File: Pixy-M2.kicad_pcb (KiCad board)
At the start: 4 copper layers, 66 x 100 mm, 57 parts, among them J10 SM09B-SRSS-TB, J4 SM06B-SRSS-TB, J5 SM06B-SRSS-TB, J6 SM06B-SRSS-TB, J7 SM06B-SRSS-TB, J8 SM06B-SRSS-TB, J9 SM06B-SRSS-TB, Q1 AO4407A, SW3 JS102011SAQN, U1 ESP32-S3-DevKitC-1-N8R8, U3 AP63203WU, U4 DRV8231ADSG, U5 DRV8231ADSG

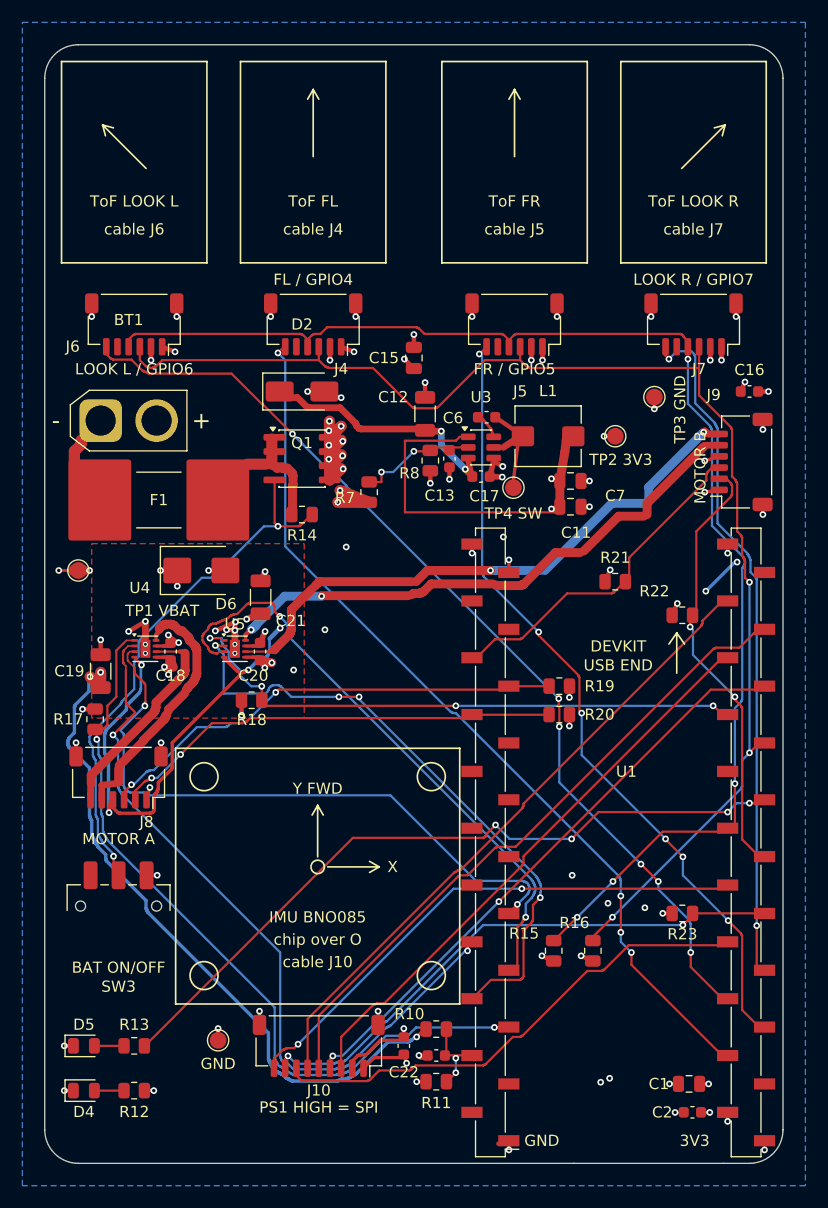
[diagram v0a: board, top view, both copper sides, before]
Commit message: layout: straighten routed copper into 0/45/90 degree runs
The A* router turns for free on its 0.05 mm grid, so any other angle came
out as a staircase of 0.05-0.3 mm steps that renders as a curve: 1060 of
the board's 1678 segments, most visibly the motor trunks round U4/U5.

New rework stage 21, tools/autoroute/octilinear.py, runs after devkit.py:
- joins pieces that meet only by overlapping, splitting the host so no
  copper moves (_heal);
- cuts each net and layer into chains between pads, vias, junctions and
  width changes, and rebuilds each as the fewest clear legs, preferring
  45 degree turns and chamfering 90 degree corners;
- tests clearance with the router's raster and the custom floors, plus
  0.02 mm, and holds 0.85 mm between IPROPI and motor copper;
- keeps each motor output within 1.5 mm of its partner, so a pair
  straightens together;
- leaves the hand-placed buck block and the piece on each U4/U5 pin, and
  keeps narrow necks inside their Motor pin escape area;
- repeats until a round changes nothing.

Result: 1678 -> 699 segments, 76 -> 15 off-angle (all hand-placed stubs).
Motor loops A 26.4 -> 25.9 mm2, B 27.8 -> 24.3 mm2. IPROPI 0.80 mm and
REG_EN 8.0 mm from motor copper, unchanged. 192 vias. DRC 0 violations /
0 unconnected / 0 parity, aperture audit passes, and a full replay
reproduces the board. Evidence in layout/octilinear/.

Docs: renders refreshed, devkit measurements updated, and CLAUDE.md's
GPIO2 floor corrected to 1.20 mm (J8's move in stage 20 set it).

Co-Authored-By: Claude Opus 5.5 <noreply@anthropic.com>
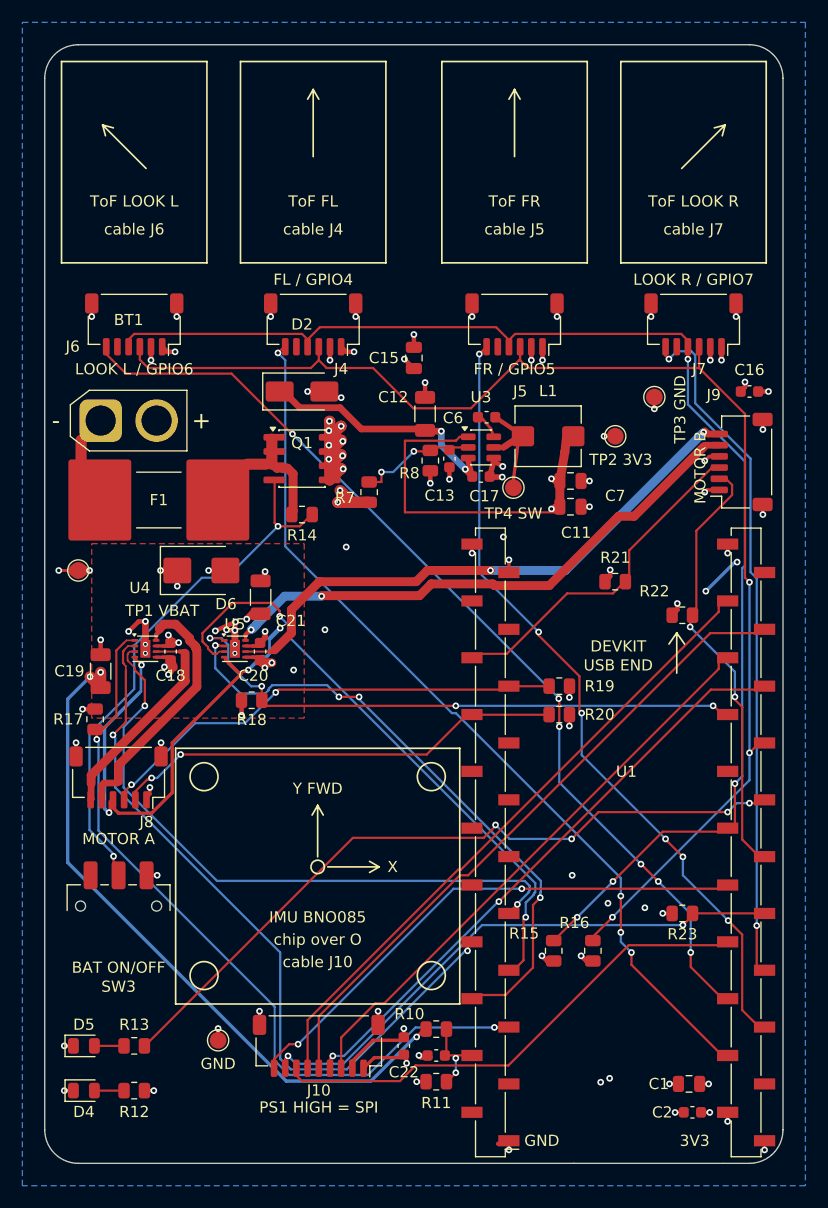
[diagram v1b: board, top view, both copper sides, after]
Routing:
- net /MOT_A_2: track 21.8 -> 23.5 mm
- net /ESP_3V3: track 102.8 -> 104.0 mm
- net /MOT_B_2: track 48.7 -> 49.8 mm
- net /GPIO42: track 55.6 -> 54.6 mm
- net /MOT_B_1: track 50.9 -> 51.7 mm
- net /VBAT: track 97.9 -> 98.7 mm
- net /GPIO40: track 66.9 -> 66.3 mm
- net GND: track 75.9 -> 76.5 mm

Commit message: power: independent motor cutoff, 1.242 V current reference, USB-priority isolation
Three supply problems on the devkit board:
- R7/R8 disable only the buck, so USB could keep the ESP32 alive and driving
  the motors from a flat pack.
- U4/U5 VREF came from the 3V3 rail, so the current limit followed the rail.
- The buck output was tied straight to the devkit's 3V3 pins, so USB and the
  buck fed one rail.

Schematic (tools/schematic/power_integrity.py; part data in
tools/power_integrity_data.py):
- U6 TLV3012B watches VBAT through R24/R25/R26 (100 k / 23.2 k / 825 k,
  0.1 %, 25 ppm/C) against its 1.242 V reference. U7 SN74LV4066A disconnects
  GPIO39-42 from the drivers below 6.35 V and reconnects them above 6.75 V,
  so the drivers' pulldowns coast both motors whatever USB or firmware do.
  The DC envelopes are 6.01-6.74 V (coast) and 6.39-7.08 V (enable).
- MOTOR_VREF from U6's REF feeds U4/U5 VREF. R17/R18 are now 1 k 1 %:
  ITRIP 0.828 A nominal, IPROPI 1.5 V/A. C25 (2.2 nF) at U6 and C28 (4.7 nF)
  at the driver split stay under the REF's 10 nF limit.
- BUCK_3V3 reaches ESP_3V3 through U8 LM66100 and Q2 AO3401A (opposing body
  diodes, Q3 following U8 ST). The devkit's 5V pin (U1.21) is sensed through
  R28/R29, giving USB priority. C30 (100 uF) carries ESP_3V3 through U8's
  turn-on at USB unplug.
- TP10 (MOTOR_OK), TP11 (MOTOR_VREF). Project symbol library Pixy-M2.kicad_sym.
- 72 nets, 79 parts, ERC 0. tools/power_integrity_check.py audits all 278
  pins, every part's fields and the DC corners.

Layout (new rework stage 21, tools/autoroute/power_integrity.py):
- The parts sit in clusters that keep the existing corridors free:
  - the USB switch in front of the devkit's USB end, fed straight from L1.2
    with no via;
  - U6/U7 and the divider at the rear, between the socket rows;
  - C28 and TP11 beside the motor corner;
  - TP2/TP3 moved between J5 and J7.
- Every re-routable net a cluster displaces is ripped whole and routed again.
  A first version patche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
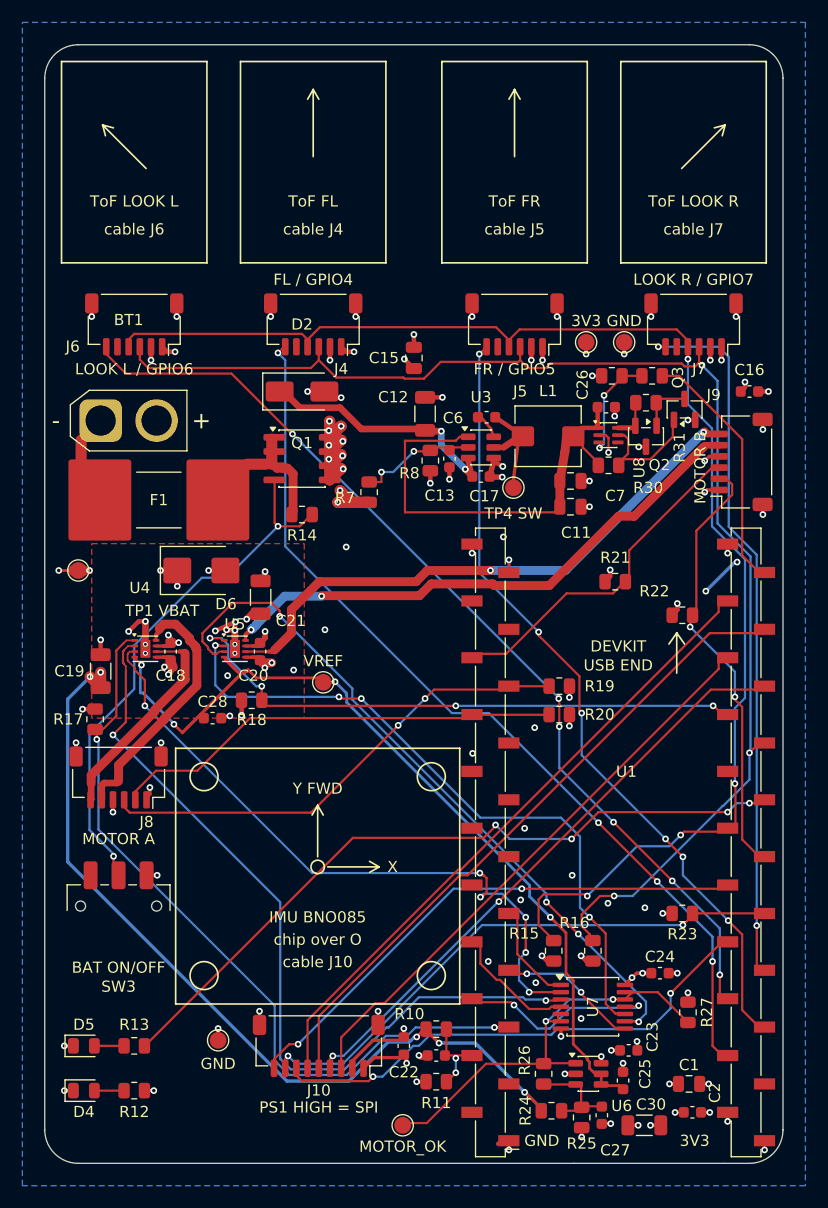
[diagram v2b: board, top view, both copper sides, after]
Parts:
- added C23: 0.1uF 16V, Capacitor_SMD:C_0603_1608Metric, F.Cu at (152.2, 149.9)
- added C24: 0.1uF 16V, Capacitor_SMD:C_0603_1608Metric, F.Cu at (155.0, 143.0)
- added C25: 2.2nF 16V, Capacitor_SMD:C_0603_1608Metric, F.Cu at (151.7, 152.6)
- added C26: 1uF 16V, Capacitor_SMD:C_0603_1608Metric, F.Cu at (150.2, 92.4)
- added C27: 0.1uF 16V, Capacitor_SMD:C_0603_1608Metric, F.Cu at (149.8, 155.7)
- added C28: 4.7nF 16V, Capacitor_SMD:C_0603_1608Metric, F.Cu at (115.0, 120.2)
- added C30: 100uF 6.3V X5R, Capacitor_SMD:C_1206_3216Metric, F.Cu at (153.6, 156.6)
- added Q2: AO3401A, Package_TO_SOT_SMD:SOT-23, F.Cu at (153.8, 95.0)
- added Q3: MMBT3904, Package_TO_SOT_SMD:SOT-23, F.Cu at (157.2, 92.6)
- added R24: 100k 0.1%, Resistor_SMD:R_0805_2012Metric, F.Cu at (145.3, 155.3)
- added R25: 23.2k 0.1%, Resistor_SMD:R_0805_2012Metric, F.Cu at (148.0, 155.9)
- added R26: 825k 0.1%, Resistor_SMD:R_0805_2012Metric, F.Cu at (144.6, 152.0)
- added R27: 100k 1%, Resistor_SMD:R_0805_2012Metric, F.Cu at (157.5, 146.5)
- added R28: 10k 1%, Resistor_SMD:R_0805_2012Metric, F.Cu at (154.3, 89.6)
- added R29: 82k 1%, Resistor_SMD:R_0805_2012Metric, F.Cu at (150.7, 89.6)
- added R30: 100k 1%, Resistor_SMD:R_0805_2012Metric, F.Cu at (150.4, 97.6)
- added R31: 100k 1%, Resistor_SMD:R_0805_2012Metric, F.Cu at (153.8, 92.0)
- added TP10: MOTOR_OK, TestPoint:TestPoint_Pad_D1.5mm, F.Cu at (132.0, 156.6)
- added TP11: MOTOR_VREF, TestPoint:TestPoint_Pad_D1.5mm, F.Cu at (124.9, 117.0)
- added U6: TLV3012B, Package_TO_SOT_SMD:SOT-23-6, F.Cu at (148.6, 152.0)
- added U7: SN74LV4066APW, Package_SO:TSSOP-14_4.4x5mm_P0.65mm, F.Cu at (149.0, 146.0)
- added U8: LM66100DCK, Package_TO_SOT_SMD:SOT-363_SC-70-6, F.Cu at (150.4, 94.9)
- R17, R18: value 2.2kOhm 1% -> 1kOhm 1%
- moved TP2 8.79 mm to (148.4, 86.6)
- moved TP3 5.59 mm to (151.8, 86.6)
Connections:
- C11 pad 1: /ESP_3V3 -> /BUCK_3V3
- C7 pad 1: /ESP_3V3 -> /BUCK_3V3
- L1 pad 2: /ESP_3V3 -> /BUCK_3V3
- U1 pad 21: unconnected-(U1-5V-Pad21) -> /DEVKIT_5V
- U3 pad 1: /ESP_3V3 -> /BUCK_3V3
- U4 pad 2: /GPIO40 -> /DRV_A_IN2
- U4 pad 3: /GPIO39 -> /DRV_A_IN1
- U4 pad 4: /ESP_3V3 -> /MOTOR_VREF
- U5 pad 2: /GPIO42 -> /DRV_B_IN2
- U5 pad 3: /GPIO41 -> /DRV_B_IN1
- U5 pad 4: /ESP_3V3 -> /MOTOR_VREF
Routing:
- net /MOTOR_VREF: track 0.00 -> 73.9 mm, vias 0 -> 4
- net /DRV_A_IN2: track 0.00 -> 72.4 mm, vias 0 -> 2
- net /ESP_3V3: track 104.0 -> 34.3 mm, vias 27 -> 28
- net /DRV_B_IN1: track 0.00 -> 63.3 mm, vias 0 -> 4
- net /DRV_A_IN1: track 0.00 -> 59.7 mm, vias 0 -> 6
- net /DRV_B_IN2: track 0.00 -> 59.7 mm, vias 0 -> 4
- net /GPIO40: track 66.3 -> 10.6 mm, vias 2 -> 0
- net /GPIO39: track 56.7 -> 8.33 mm, vias 2 -> 0
- net /GPIO41: track 53.4 -> 11.1 mm
- net /GPIO42: track 54.6 -> 17.2 mm, vias 4 -> 2
- net /BUCK_3V3: track 0.00 -> 37.4 mm
- net /MOTOR_OK: track 0.00 -> 35.7 mm, vias 0 -> 2
- net /DEVKIT_5V: track 0.00 -> 21.2 mm
- net GND: track 76.5 -> 89.5 mm, vias 72 -> 92
- net /VBAT: track 98.7 -> 111.0 mm, vias 24 -> 26
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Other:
- board text added: "3V3"
- board text added: "MOTOR_OK"
- board text added: "VREF"
- board text removed: "TP2 3V3"
- board text removed: "TP3 GND"
